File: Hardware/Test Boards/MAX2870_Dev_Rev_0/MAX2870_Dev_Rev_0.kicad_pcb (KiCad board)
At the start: 4 copper layers, 49 x 49 mm, 50 parts, among them J1 Conn_02x05_Odd_Even, J2 SMA, U1 AMS1117-3.3, U2 LP5907MFX-3.3, U3 MAX2871, U4 MIC5366-1.8

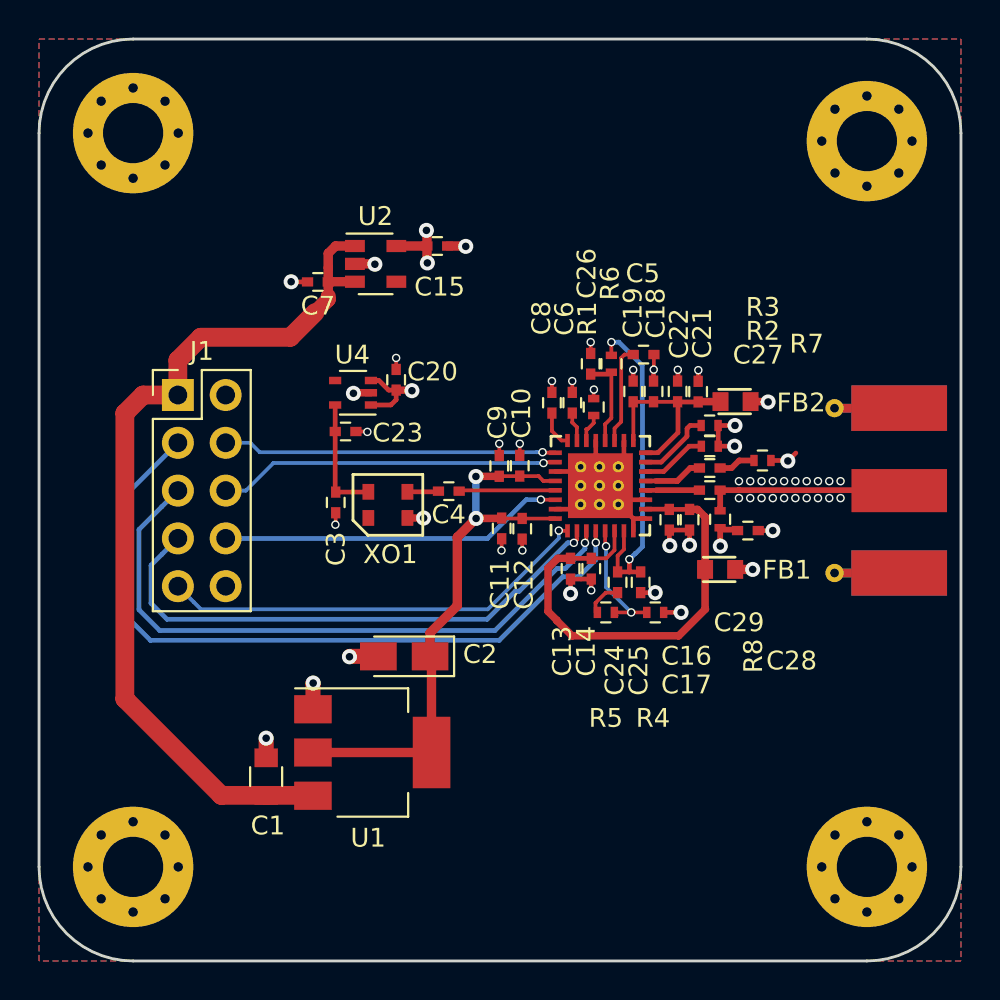
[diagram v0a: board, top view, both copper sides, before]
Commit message: Finished MAX2870 layout, added 3D models and licence
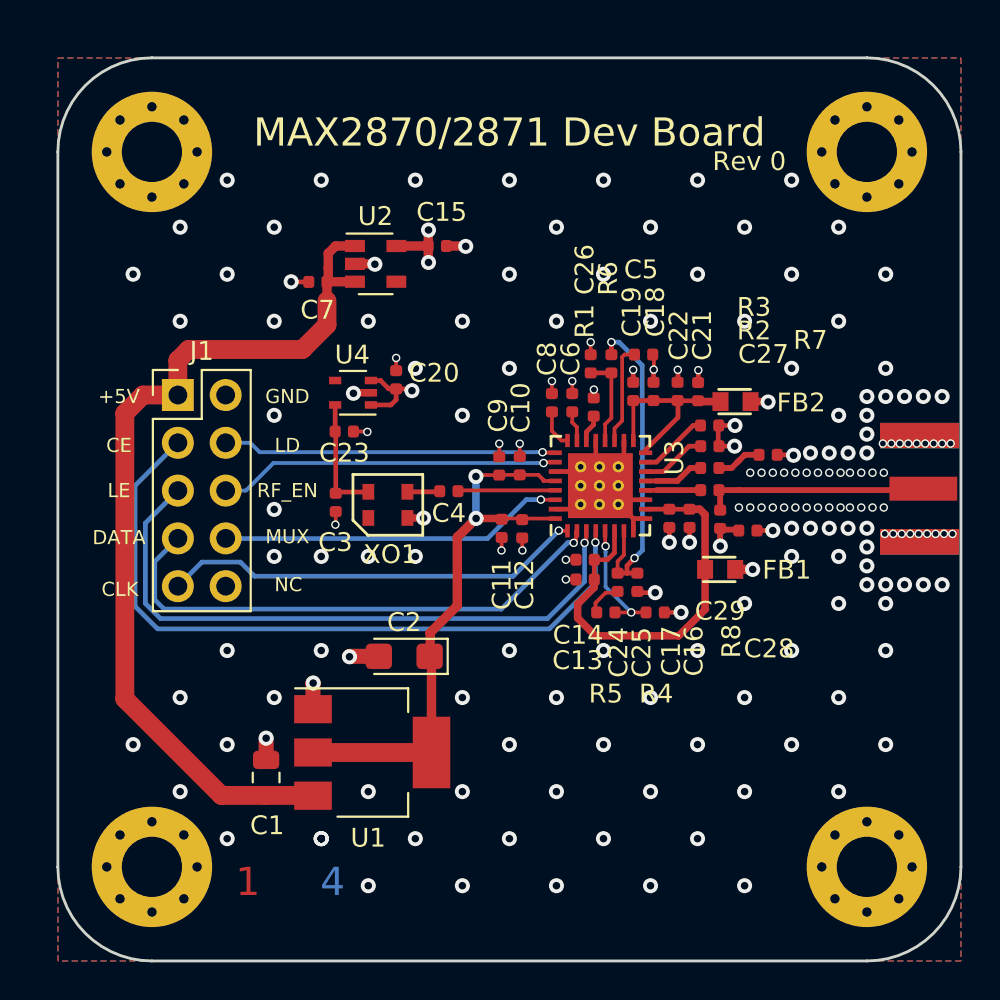
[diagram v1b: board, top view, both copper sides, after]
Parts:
- added ?: , VNA_Footprints:OSHW_Logo_3.6x3.6_F.Mask, F.Cu at (75.0, 109.8)
- added REF**: 4LayerCheck, VNA_Footprints:4LayerCheck, F.Cu at (68.6, 109.8)
- C1: footprint Capacitors_SMD:C_0805 -> Capacitor_SMD:C_0805_2012Metric
- C10, C11, C12, C13, C14, C15, C16, C17, C18, C19, C20, C21, C22, C23, C24, C25, C26, C27, C28, C29, C3, C4, C5, C6, C7, C8, C9: footprint Capacitors_SMD:C_0402 -> Capacitor_SMD:C_0402_1005Metric
- C2: footprint Capacitors_Tantalum_SMD:CP_Tantalum_Case-A_EIA-3216-18_Reflow -> Capacitor_Tantalum_SMD:CP_EIA-3216-18_Kemet-A
- H1, H2, H3, H4: footprint Mounting_Holes:MountingHole_3.2mm_M3_Pad_Via -> MountingHole:MountingHole_3.2mm_M3_Pad_Via
- J1: footprint Pin_Headers:Pin_Header_Straight_2x05_Pitch2.54mm -> Connector_PinHeader_2.54mm:PinHeader_2x05_P2.54mm_Vertical
- J2: footprint Connectors_Molex:Molex_SMA_Jack_Edge_Mount -> VNA_Footprints:SMA_EDGE_MOUNT
- R1, R2, R3, R4, R5, R6, R7, R8: footprint Resistors_SMD:R_0402 -> Resistor_SMD:R_0402_1005Metric
- U1: footprint TO_SOT_Packages_SMD:SOT-223-3_TabPin2 -> Package_TO_SOT_SMD:SOT-223-3_TabPin2
- U2: footprint TO_SOT_Packages_SMD:SOT-23-5 -> Package_TO_SOT_SMD:SOT-23-5
- U4: footprint TO_SOT_Packages_SMD:SOT-353_SC-70-5 -> Package_TO_SOT_SMD:SOT-353_SC-70-5
- moved J2 2.80 mm to (101.8, 88.9), turned to 0 degrees
- moved H1 1.41 mm to (61.0, 71.0)
- moved H2 1.00 mm to (61.0, 109.0)
- moved C13 0.97 mm to (84.0, 93.7), turned to 180 degrees
- moved C14 0.58 mm to (84.0, 92.7), turned to 180 degrees
- moved H4 0.57 mm to (99.0, 71.0)
- moved R7 0.42 mm to (93.8, 87.1)
- moved C25 0.17 mm to (86.8, 93.9)
- moved C16 0.08 mm to (89.6, 90.5)
- moved C17 0.08 mm to (88.5, 90.5)
- moved C23 0.07 mm to (71.2, 85.9)
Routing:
- net /3v3_PLL: track 25.2 -> 22.0 mm
- net GND: track 38.4 -> 35.3 mm, vias 51 -> 185
- net /DATA: track 29.3 -> 28.4 mm
- net +5V: track 47.2 -> 48.0 mm
- net /CE: track 39.1 -> 38.4 mm
- net /CLK: track 23.2 -> 22.6 mm
- net Net-(C27-Pad1): track 1.97 -> 2.53 mm
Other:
- board size 49 x 49 mm -> 48 x 48 mm
- board text added: "+5V"
- board text added: "CE"
- board text added: "CLK"
- board text added: "DATA"
- board text added: "GND"
- board text added: "Josh Johnson"
- board text added: "LD"
- board text added: "LE"
- board text added: "MAX2870/2871 Dev Board"
- board text added: "MUX"
- board text added: "NC"
- board text added: "RF_EN"
- board text added: "Rev 0"
- board text added: "github.com/joshajohnson/vna"
- board text added: "joshajohnson.com"

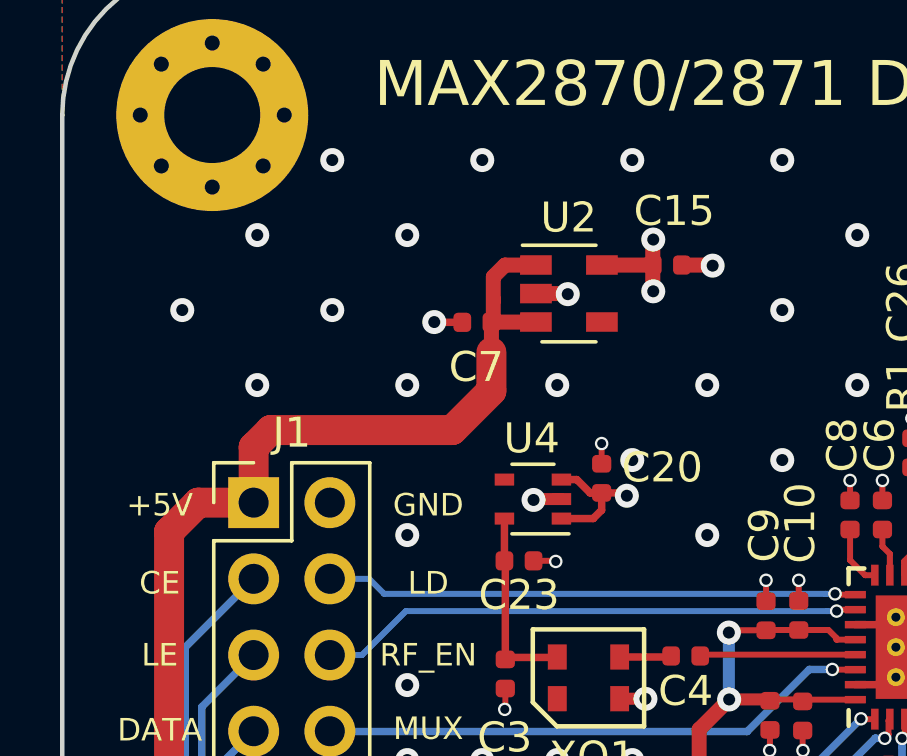
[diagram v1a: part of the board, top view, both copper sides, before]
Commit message: Changed 3v3 reg position on MAX2870 dev board
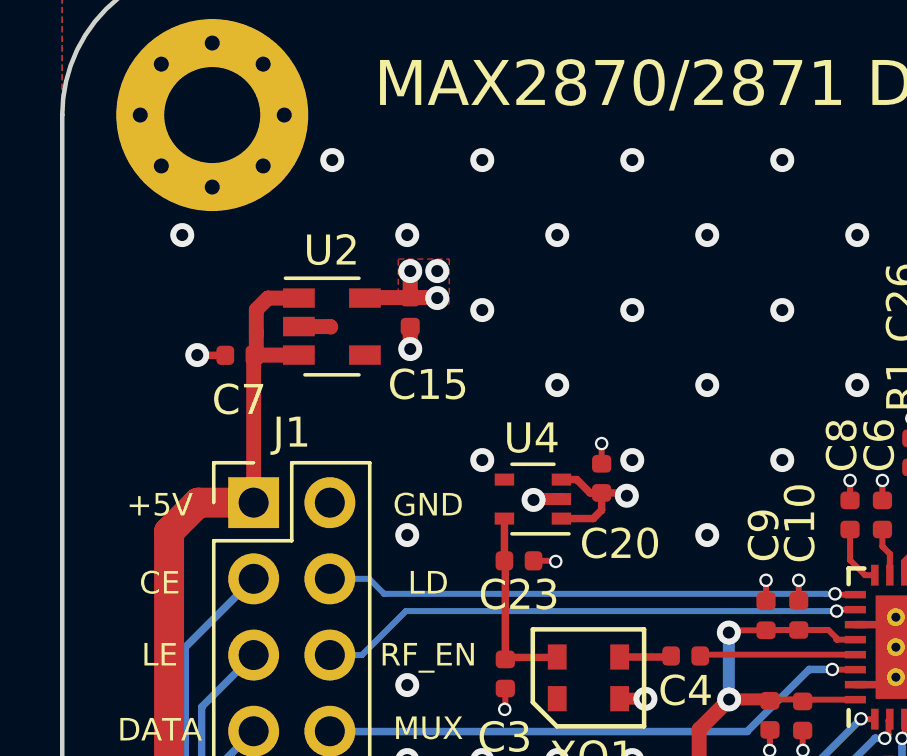
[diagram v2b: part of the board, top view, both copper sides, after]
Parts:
- moved C15 8.71 mm to (67.6, 77.6), turned to 270 degrees
- moved U2 7.98 mm to (65.0, 78.0)
- moved C7 7.98 mm to (61.9, 79.0)
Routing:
- net +5V: track 48.0 -> 40.0 mm
- net +3.3VA: track 14.2 -> 14.0 mm, vias 8 -> 9
- added copper zone on F.Cu, net +3.3VA

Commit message: Finalised Gerbers to be sent off to the fab
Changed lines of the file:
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@@
     (thickness 1.6)
     (drawings 23)
-    (tracks 520)
+    (tracks 521)
     (zones 0)
     (modules 52)
@@
   (segment (start 72.64 83.8) (end 71.74 83.8) (width 0.4) (layer F.Cu) (net 1))
   (segment (start 71.74 83.8) (end 71.71 83.83) (width 0.4) (layer F.Cu) (net 1))
-  (via (at 73.98 81.95) (size 0.45) (drill 0.3) (layers F.Cu B.Cu) (net 1))
-  (segment (start 73.98 82.56) (end 73.98 81.95) (width 0.2) (layer F.Cu) (net 1))
   (via (at 70.75 90.81) (size 0.45) (drill 0.3) (layers F.Cu B.Cu) (net 1))
   (segment (start 70.77 90.18) (end 70.77 90.79) (width 0.2) (layer F.Cu) (net 1))
@@
   (via (at 70 77.5) (size 0.8) (drill 0.4) (layers F.Cu B.Cu) (net 1))
   (via (at 70 82.5) (size 0.8) (drill 0.4) (layers F.Cu B.Cu) (net 1))
+  (via (at 74 81.8) (size 0.8) (drill 0.4) (layers F.Cu B.Cu) (net 1))
+  (segment (start 73.98 81.82) (end 74 81.8) (width 0.25) (layer F.Cu) (net 1))
+  (segment (start 73.98 82.625) (end 73.98 81.82) (width 0.25) (layer F.Cu) (net 1))
   (segment (start 62.51 79) (end 62.47 79.04) (width 0.4) (layer F.Cu) (net 2))
   (segment (start 62.48 79) (end 62.47 79.01) (width 0.5) (layer F.Cu) (net 2))
